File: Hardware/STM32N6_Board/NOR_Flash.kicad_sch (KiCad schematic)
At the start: 16 parts, among them U7 MX25LM51245GXDI00, U8 SPX5205-ADJ

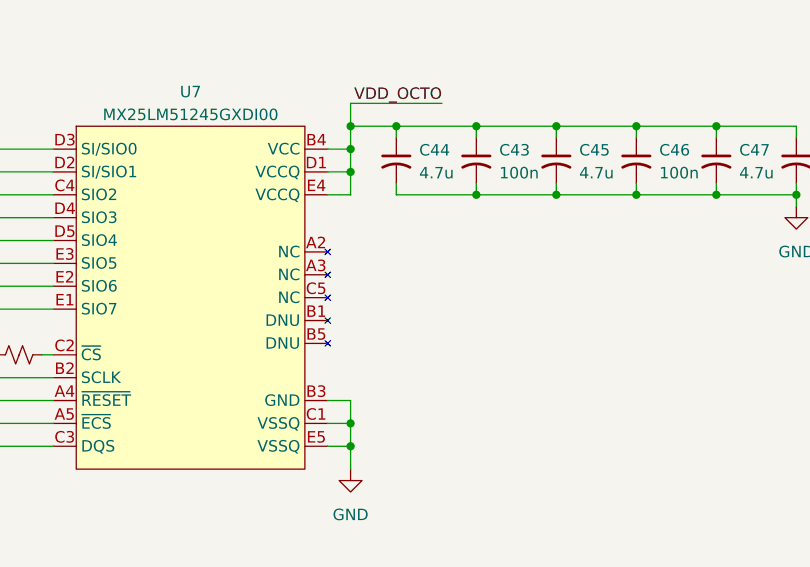
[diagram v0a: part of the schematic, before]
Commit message: added decoupling caps and other stuffs
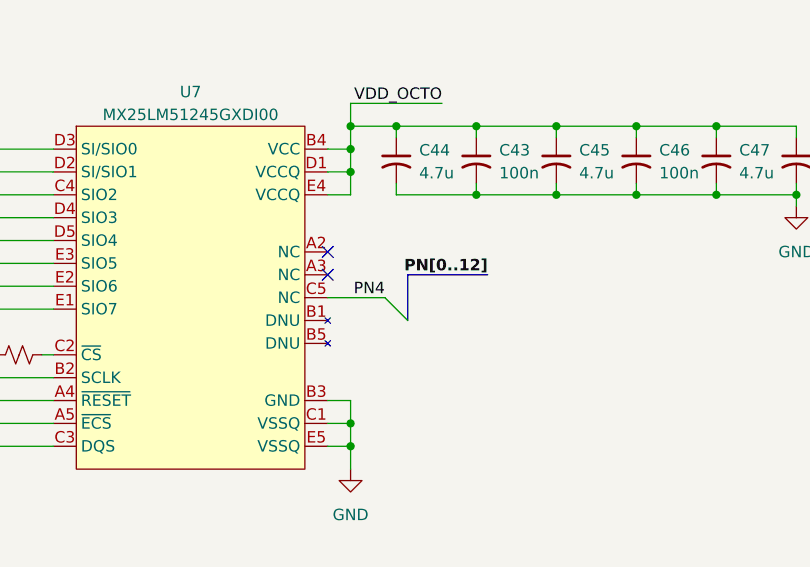
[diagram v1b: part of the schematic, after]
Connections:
- net PN4: now also U7.C5 (NC)
- no-connect marks 0 -> 2
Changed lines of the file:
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@@
 		(color 0 0 0 0)
+	)
+	(no_connect
+		(at 92.71 49.53)
+	)
+	(no_connect
+		(at 92.71 46.99)
 	)
 	(bus_entry
@@
 	)
 	(bus_entry
+		(at 101.6 54.61)
+		(size -2.54 -2.54)
+		(stroke
+			(width 0)
+			(type default)
+		)
+	)
+	(bus_entry
 		(at 49.53 58.42)
 		(size -2.54 -2.54)
@@
 	(bus
 		(pts
+			(xy 101.6 49.53) (xy 101.6 54.61)
+		)
+		(stroke
+			(width 0)
+			(type default)
+		)
+	)
+	(bus
+		(pts
 			(xy 46.99 33.02) (xy 46.99 35.56)
 		)
@@
 	(wire
 		(pts
+			(xy 92.71 52.07) (xy 99.06 52.07)
+		)
+		(stroke
+			(width 0)
+			(type default)
+		)
+	)
+	(wire
+		(pts
 			(xy 74.93 172.72) (xy 83.82 172.72)
 		)
@@
 		(pts
 			(xy 92.71 35.56) (xy 95.25 35.56)
+		)
+		(stroke
+			(width 0)
+			(type default)
+		)
+	)
+	(bus
+		(pts
+			(xy 101.6 49.53) (xy 110.49 49.53)
 		)
 		(stroke
@@
 		)
 	)
+	(label "PN4"
+		(at 99.06 52.07 180)
+		(effects
+			(font
+				(size 1.27 1.27)
+			)
+			(justify right bottom)
+		)
+	)
 	(label "VDD_OCTO"
 		(at 92.71 121.92 180)
@@
 		)
 	)
+	(label "PN[0..12]"
+		(at 110.49 49.53 180)
+		(effects
+			(font
+				(size 1.27 1.27)
+				(thickness 0.254)
+				(bold yes)
+			)
+			(justify right bottom)
+		)
+	)

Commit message: almost finished with the board
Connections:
- net VDD_OCTO: no longer R14.2, R16.2, R17.2
- new net VDD: R14.2, R16.2, R17.2
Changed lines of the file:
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@@
-	(wire
-		(pts
-			(xy 120.65 114.3) (xy 133.35 114.3)
-		)
-		(stroke
-			(width 0)
-			(type default)
-		)
-	)
 	(wire
 		(pts
@@
 	(wire
 		(pts
-			(xy 80.01 121.92) (xy 92.71 121.92)
+			(xy 80.01 121.92) (xy 85.09 121.92)
 		)
 		(stroke
@@
 	(wire
 		(pts
-			(xy 80.01 110.49) (xy 92.71 110.49)
+			(xy 120.65 114.3) (xy 127 114.3)
+		)
+		(stroke
+			(width 0)
+			(type default)
+		)
+	)
+	(wire
+		(pts
+			(xy 80.01 110.49) (xy 85.09 110.49)
 		)
 		(stroke
@@
 		)
 	)
-	(label "VDD_OCTO"
-		(at 133.35 114.3 180)
-		(effects
-			(font
-				(size 1.27 1.27)
-			)
-			(justify right bottom)
-		)
-	)
 	(label "PWR_ON"
 		(at 195.58 54.61 0)
@@
 		)
 	)
-	(label "VDD_OCTO"
-		(at 92.71 121.92 180)
-		(effects
-			(font
-				(size 1.27 1.27)
-			)
-			(justify right bottom)
-		)
-	)
 	(label "{XSPI}"
 		(at 195.58 48.26 0)
@@
 		)
 	)
-	(label "VDD_OCTO"
-		(at 92.71 110.49 180)
-		(effects
-			(font
-				(size 1.27 1.27)
-			)
-			(justify right bottom)
-		)
-	)
 	(label "PN2"
 		(at 49.53 35.56 0)
@@
 		)
 	)
+	(global_label "VDD"
+		(shape input)
+		(at 127 114.3 0)
+		(fields_autoplaced yes)
+		(effects
+			(font
+				(size 1.27 1.27)
+			)
+			(justify left)
+		)
+		(property "Intersheetrefs" "${INTERSHEET_REFS}"
+			(at 133.6138 114.3 0)
+			(effects
+				(font
+					(size 1.27 1.27)
+				)
+				(justify left)
+				(hide yes)
+			)
+		)
+	)
+	(global_label "VDD"
+		(shape input)
+		(at 85.09 121.92 0)
+		(fields_autoplaced yes)
+		(effects
+			(font
+				(size 1.27 1.27)
+			)
+			(justify left)
+		)
+		(property "Intersheetrefs" "${INTERSHEET_REFS}"
+			(at 91.7038 121.92 0)
+			(effects
+				(font
+					(size 1.27 1.27)
+				)
+				(justify left)
+				(hide yes)
+			)
+		)
+	)
+	(global_label "VDD"
+		(shape input)
+		(at 85.09 110.49 0)
+		(fields_autoplaced yes)
+		(effects
+			(font
+				(size 1.27 1.27)
+			)
+			(justify left)
+		)
+		(property "Intersheetrefs" "${INTERSHEET_REFS}"
+			(at 91.7038 110.49 0)
+			(effects
+				(font
+					(size 1.27 1.27)
+				)
+				(justify left)
+				(hide yes)
+			)
+		)
+	)

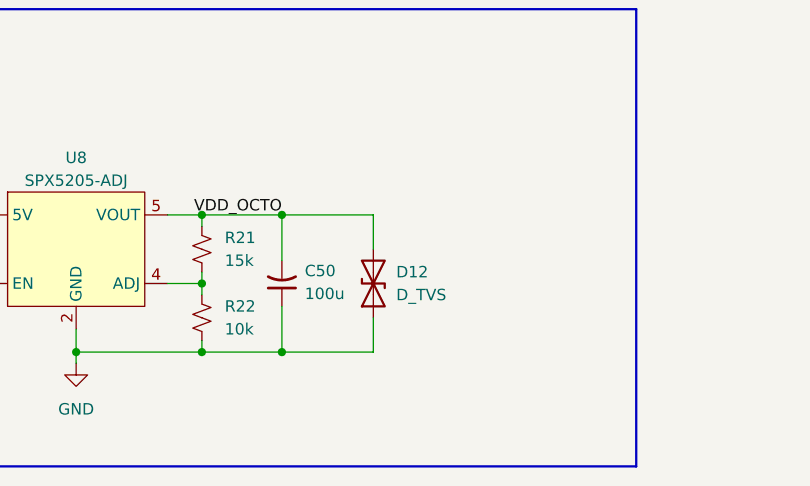
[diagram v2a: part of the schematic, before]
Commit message: Added the gerbers, drill files, BOM, and CPL files
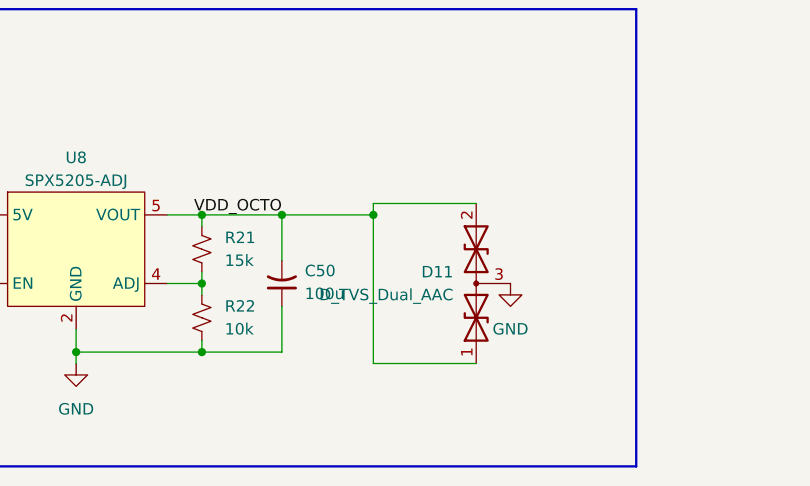
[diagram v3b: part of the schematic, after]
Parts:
- removed D12: D_TVS, LED_SMD:LED_0805_2012Metric_Pad1.15x1.40mm_HandSolder, symbol Device:D_TVS
- added D11: D_TVS_Dual_AAC, Package_TO_SOT_SMD:SOT-723, symbol Device:D_TVS_Dual_AAC
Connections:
- net GND: now also D11.3 (common)
- net VDD_OCTO: now also D11.1 (A1), D11.2 (A2)
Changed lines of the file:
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@@
+	)
+	(junction
+		(at 127 165.1)
+		(diameter 0)
+		(color 0 0 0 0)
 	)
 	(junction
@@
 	)
 	(junction
-		(at 116.84 180.34)
-		(diameter 0)
-		(color 0 0 0 0)
-	)
-	(junction
 		(at 95.25 38.1)
 		(diameter 0)
@@
 		)
 	)
+	(wire
+		(pts
+			(xy 138.43 163.83) (xy 127 163.83)
+		)
+		(stroke
+			(width 0)
+			(type default)
+		)
+	)
 	(polyline
 		(pts
@@
 	(wire
 		(pts
-			(xy 127 168.91) (xy 127 165.1)
+			(xy 127 165.1) (xy 127 181.61)
 		)
 		(stroke
@@
 		)
 	)
+	(wire
+		(pts
+			(xy 138.43 181.61) (xy 127 181.61)
+		)
+		(stroke
+			(width 0)
+			(type default)
+		)
+	)
 	(bus
 		(pts
@@
 	(wire
 		(pts
+			(xy 127 163.83) (xy 127 165.1)
+		)
+		(stroke
+			(width 0)
+			(type default)
+		)
+	)
+	(wire
+		(pts
 			(xy 118.11 39.37) (xy 118.11 40.64)
 		)
@@
 	(wire
 		(pts
-			(xy 127 180.34) (xy 116.84 180.34)
-		)
-		(stroke
-			(width 0)
-			(type default)
-		)
-	)
-	(wire
-		(pts
 			(xy 81.28 165.1) (xy 83.82 165.1)
 		)
@@
 		(pts
 			(xy 67.31 110.49) (xy 74.93 110.49)
-		)
-		(stroke
-			(width 0)
-			(type default)
-		)
-	)
-	(wire
-		(pts
-			(xy 127 176.53) (xy 127 180.34)
 		)
 		(stroke
@@
 			)
 			(justify left)
+		)
+	)
+	(symbol
+		(lib_id "Device:D_TVS_Dual_AAC")
+		(at 138.43 172.72 90)
+		(unit 1)
+		(exclude_from_sim no)
+		(in_bom yes)
+		(on_board yes)
+		(dnp no)
+		(fields_autoplaced yes)
+		(property "Reference" "D11"
+			(at 135.89 171.4499 90)
+			(effects
+				(font
+					(size 1.27 1.27)
+				)
+				(justify left)
+			)
+		)
+		(property "Value" "D_TVS_Dual_AAC"
+			(at 135.89 173.9899 90)
+			(effects
+				(font
+					(size 1.27 1.27)
+				)
+				(justify left)
+			)
+		)
+		(property "Footprint" "Package_TO_SOT_SMD:SOT-723"
+			(at 138.43 176.53 0)
+			(effects
+				(font
+					(size 1.27 1.27)
+				)
+				(hide yes)
+			)
+		)
+		(property "Datasheet" "~"
+			(at 138.43 176.53 0)
+			(effects
+				(font
+					(size 1.27 1.27)
+				)
+				(hide yes)
+			)
+		)
+		(property "Description" "Bidirectional dual transient-voltage-suppression diode, center on pin 3"
+			(at 138.43 172.72 0)
+			(effects
+				(font
+					(size 1.27 1.27)
+				)
+				(hide yes)
+			)
+		)
+		(pin "1"
+		)
+		(pin "3"
+		)
+		(pin "2"
+		)
+		(instances
+			(project ""
+				(path "/4869b3db-9bd3-4900-9c3c-205f01100fa6/6b6613e8-e0b6-4175-a413-8c927f6f4831"
+					(reference "D11")
+					(unit 1)
+				)
+			)
 		)
 	)
@@
 	)
 	(symbol
+		(lib_id "power:GND")
+		(at 142.24 172.72 0)
+		(unit 1)
+		(exclude_from_sim no)
+		(in_bom yes)
+		(on_board yes)
+		(dnp no)
+		(fields_autoplaced yes)
+		(property "Reference" "#PWR071"
+			(at 142.24 179.07 0)
+			(effects
+				(font
+					(size 1.27 1.27)
+				)
+				(hide yes)
+			)
+		)
+		(property "Value" "GND"
+			(at 142.24 177.8 0)
+			(effects
+				(font
+					(size 1.27 1.27)
+				)
+			)
+		)
+		(property "Footprint" ""
+			(at 142.24 172.72 0)
+			(effects
+				(font
+					(size 1.27 1.27)
+				)
+				(hide yes)
+			)
+		)
+		(property "Datasheet" ""
+			(at 142.24 172.72 0)
+			(effects
+				(font
+					(size 1.27 1.27)
+				)
+				(hide yes)
+			)
+		)
+		(property "Description" "Power symbol creates a global label with name \"GND\" , ground"
+			(at 142.24 172.72 0)
+			(effects
+				(font
+					(size 1.27 1.27)
+				)
+				(hide yes)
+			)
+		)
+		(pin "1"
+		)
+		(instances
+			(project "STM32N6_Board"
+				(path "/4869b3db-9bd3-4900-9c3c-205f01100fa6/6b6613e8-e0b6-4175-a413-8c927f6f4831"
+					(reference "#PWR071")
+					(unit 1)
+				)
+			)
+		)
+	)
+	(symbol
 		(lib_id "power:+5V")
 		(at 81.28 162.56 0)
@@
 					(unit 1)
 				)
-			)
-		)
-	)
-	(symbol
-		(lib_id "Device:D_TVS")
-		(at 127 172.72 90)
-		(unit 1)
-		(exclude_from_sim no)
-		(in_bom yes)
-		(on_board yes)
-		(dnp no)
-		(fields_autoplaced yes)
-		(property "Reference" "D12"
-			(at 129.54 171.4499 90)
-			(effects
-				(font
-					(size 1.27 1.27)
-				)
-				(justify right)
-			)
-		)
-		(property "Value" "D_TVS"
-			(at 129.54 173.9899 90)
-			(effects
-				(font
-					(size 1.27 1.27)
-				)
-				(justify right)
-			)
-		)
-		(property "Footprint" "LED_SMD:LED_0805_2012Metric_Pad1.15x1.40mm_HandSolder"
-			(at 127 172.72 0)
-			(effects
-				(font
-					(size 1.27 1.27)
-				)
-				(hide yes)
-			)
-		)
-		(property "Datasheet" "~"
-			(at 127 172.72 0)
-			(effects
-				(font
-					(size 1.27 1.27)
-				)
-				(hide yes)
-			)
-		)
-		(property "Description" "Bidirectional transient-voltage-suppression diode"
-			(at 127 172.72 0)
-			(effects
-				(font
-					(size 1.27 1.27)
-				)
-				(hide yes)
-			)
-		)
-		(pin "1"
-		)
-		(pin "2"
-		)
-		(instances
-			(project "STM32N6_Board"
-				(path "/4869b3db-9bd3-4900-9c3c-205f01100fa6/6b6613e8-e0b6-4175-a413-8c927f6f4831"
-					(reference "D12")
-					(unit 1)
-				)
